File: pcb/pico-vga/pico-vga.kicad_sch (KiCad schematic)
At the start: 28 parts

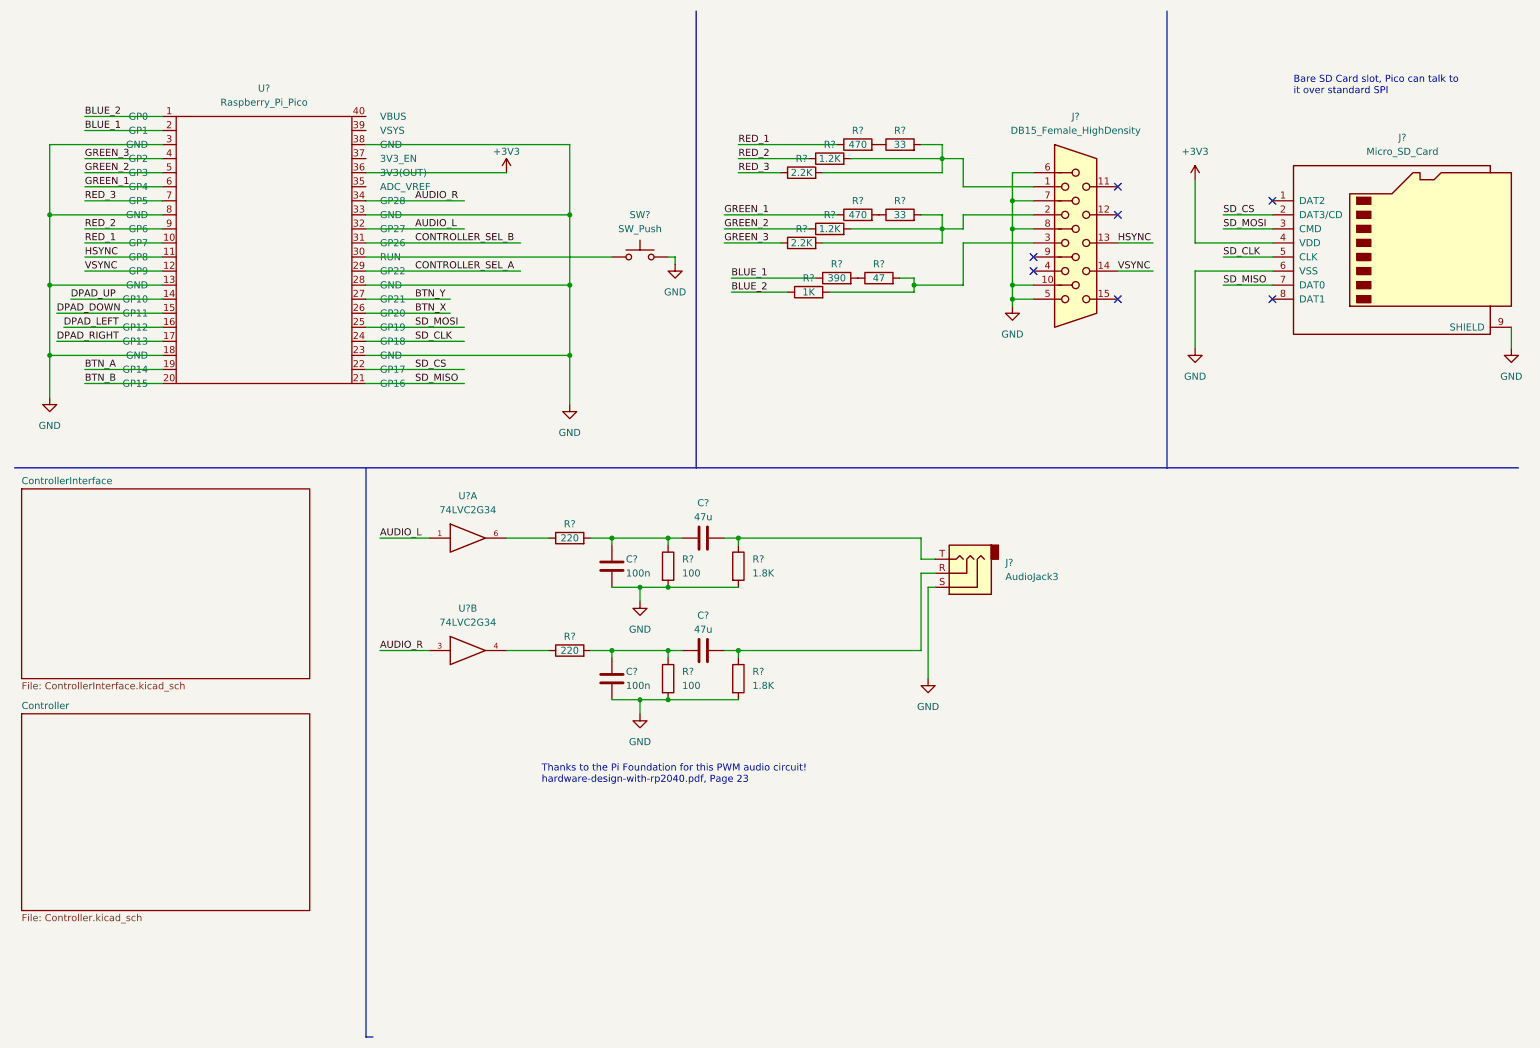
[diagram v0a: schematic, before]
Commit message: schematic completely finished, passes ERC, fully labeled
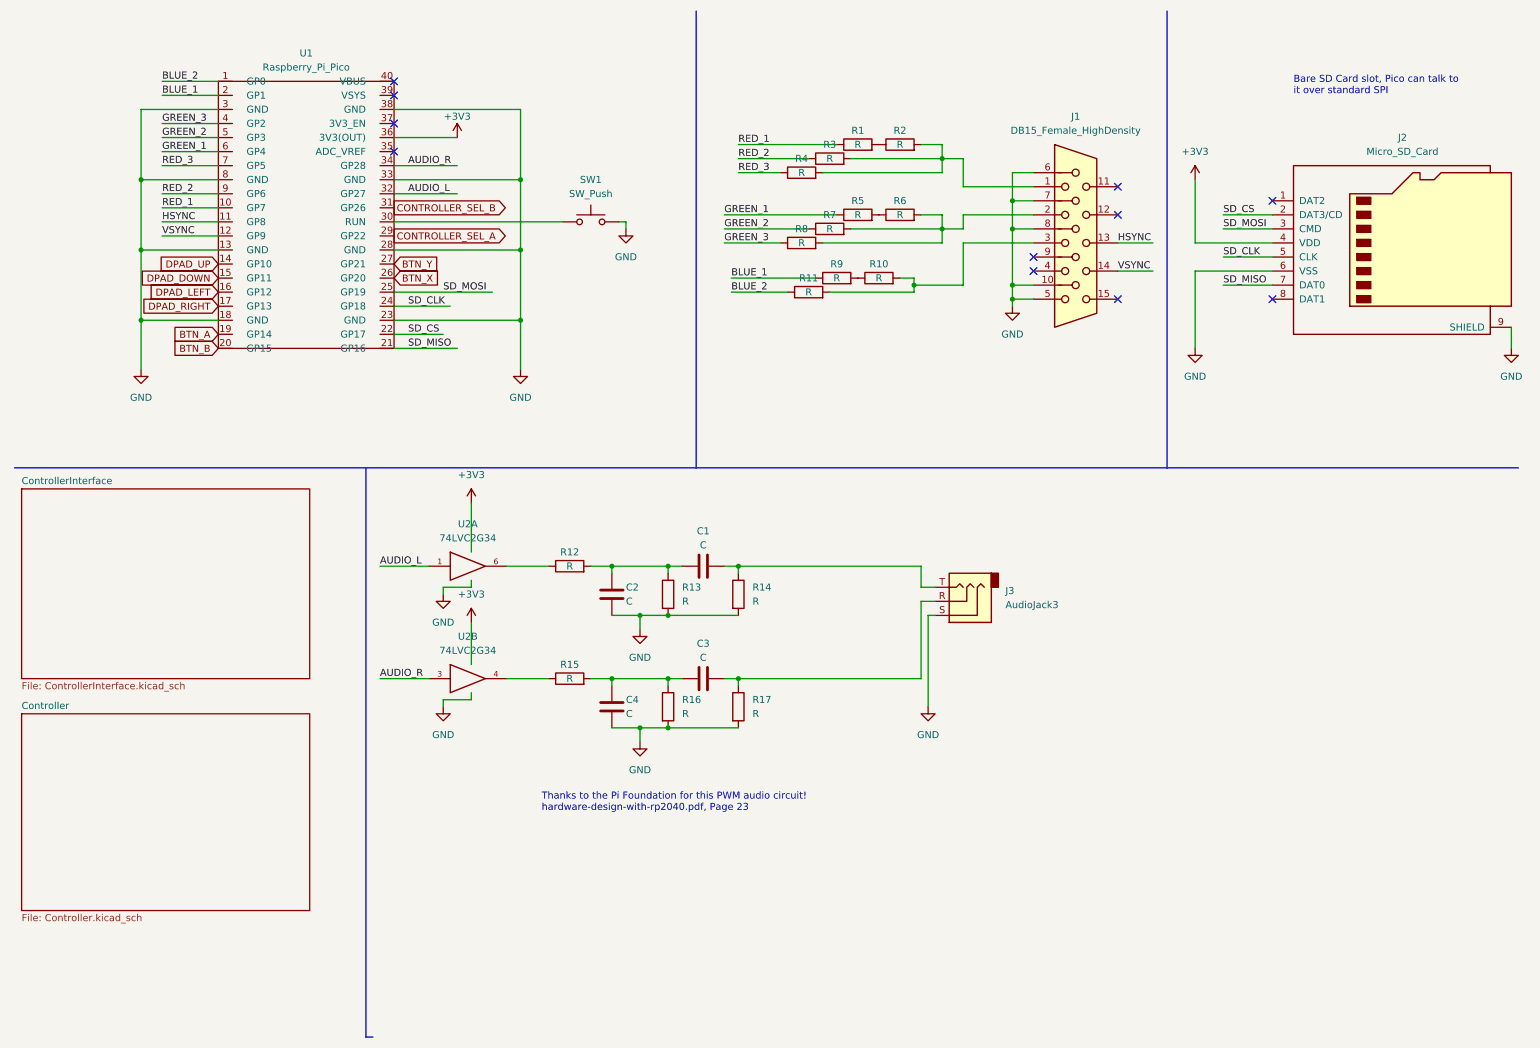
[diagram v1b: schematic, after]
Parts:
- C1, C3: renamed from C?; value 47u -> C
- C2, C4: renamed from C?; value 100n -> C
- R1, R5: renamed from R?; value 470 -> R
- R10: renamed from R?; value 47 -> R
- R11: renamed from R?; value 1K -> R
- R12, R15: renamed from R?; value 220 -> R
- R13, R16: renamed from R?; value 100 -> R
- R14, R17: renamed from R?; value 1.8K -> R
- R2, R6: renamed from R?; value 33 -> R
- R3, R7: renamed from R?; value 1.2K -> R
- R4, R8: renamed from R?; value 2.2K -> R
- R9: renamed from R?; value 390 -> R
- gave numbers to parts that had none: 6
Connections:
- net VCC is gone; now on net +3V3: U2.5 (VCC), U2.5 (VCC)
- net +3V3: now also U1.36 (3V3(OUT))
- net AUDIO_L: now also U1.32 (GP27)
- net AUDIO_R: now also U1.34 (GP28)
- net BLUE_1: now also U1.2 (GP1)
- net BLUE_2: now also U1.1 (GP0)
- net BTN_A: now also U1.19 (GP14)
- net BTN_B: now also U1.20 (GP15)
- net BTN_X: now also U1.26 (GP20)
- net BTN_Y: now also U1.27 (GP21)
- net CONTROLLER_SEL_A: now also U1.29 (GP22)
- net CONTROLLER_SEL_B: now also U1.31 (GP26)
- net DPAD_DOWN: now also U1.15 (GP11)
- net DPAD_LEFT: now also U1.16 (GP12)
- net DPAD_RIGHT: now also U1.17 (GP13)
- net DPAD_UP: now also U1.14 (GP10)
- net GND: now also U1.13 (GND), U1.18 (GND), U1.23 (GND), U1.28 (GND), U1.3 (GND), U1.33 (GND), U1.38 (GND), U1.8 (GND)
- net GREEN_1: now also U1.6 (GP4)
- net GREEN_2: now also U1.5 (GP3)
- net GREEN_3: now also U1.4 (GP2)
- net HSYNC: now also U1.11 (GP8)
- net RED_1: now also U1.10 (GP7)
- net RED_2: now also U1.9 (GP6)
- net RED_3: now also U1.7 (GP5)
- net SD_CLK: now also U1.24 (GP18)
- net SD_CS: now also U1.22 (GP17)
- net SD_MISO: now also U1.21 (GP16)
- net SD_MOSI: now also U1.25 (GP19)
- net VSYNC: now also U1.12 (GP9)
- net at U1.30 (RUN): now also SW1.1
- no-connect marks 7 -> 11
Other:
- moved on the sheet: C1, C2, C3, C4, J3, R12, R13, R14, R15, R16, R17, SW1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

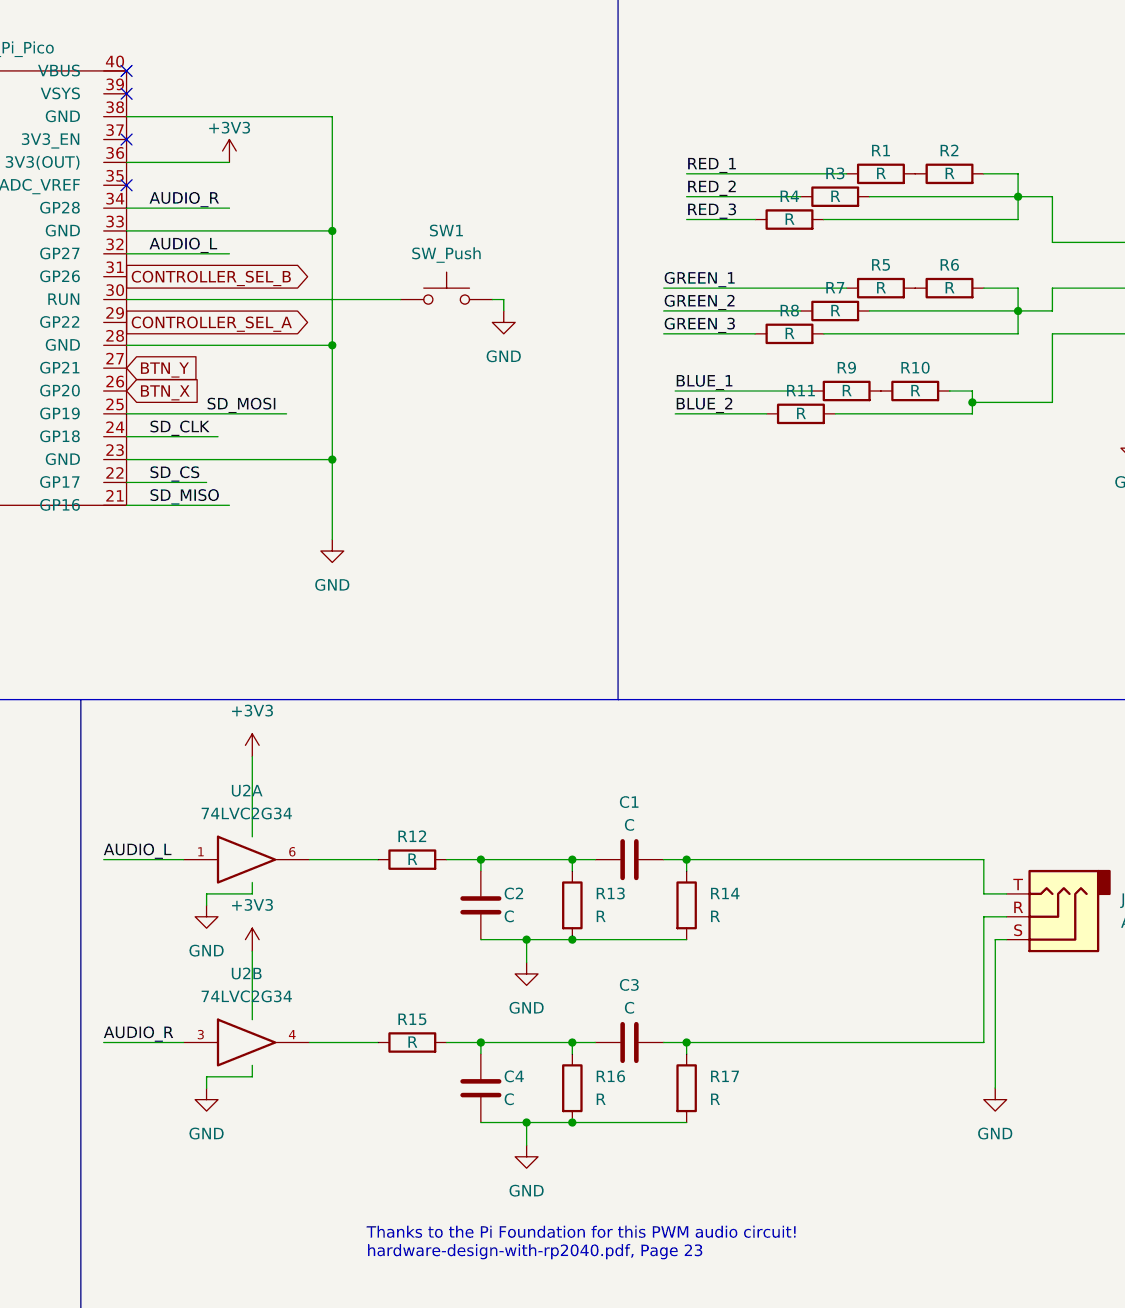
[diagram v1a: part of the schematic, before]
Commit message: NOW it's complete
kicad decided to delete all of my resistor/cap values sometime before the last commit... values are back now, everything's labeled, passes ERC
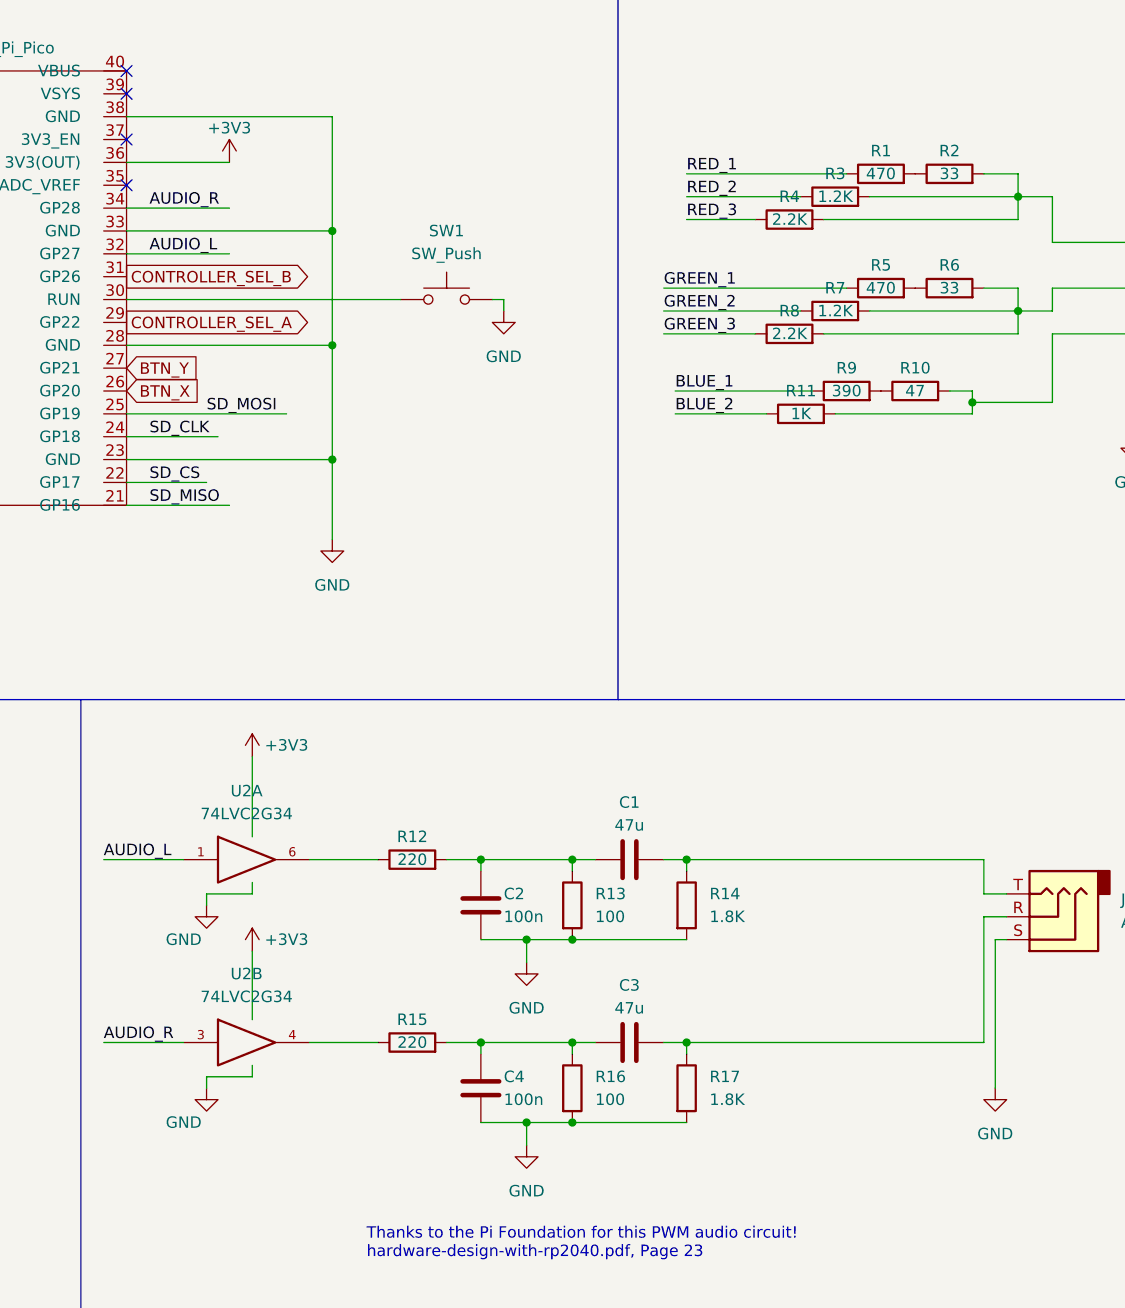
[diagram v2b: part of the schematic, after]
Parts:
- C1, C3: value C -> 47u
- C2, C4: value C -> 100n
- R1, R5: value R -> 470
- R10: value R -> 47
- R11: value R -> 1K
- R12, R15: value R -> 220
- R13, R16: value R -> 100
- R14, R17: value R -> 1.8K
- R2, R6: value R -> 33
- R3, R7: value R -> 1.2K
- R4, R8: value R -> 2.2K
- R9: value R -> 390
